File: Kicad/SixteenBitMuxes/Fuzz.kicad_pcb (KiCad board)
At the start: 2 copper layers, 100 x 82 mm, 109 parts, among them J1 Audio In/Out JST XH, J10 Key Pad JST XH, J11 LCD JST XH, J12 Bypass Switch JST XH, J2 POT B10K JST XH, J3 POT B5K JST XH, J4 VOL POT A100K JST XH, J5 PowerTest_PinHeader, J6 9V Power JST XH, J7 Boot Reset PinHeader, J9 SWD_PinHeader, Q1 PN2222A, Q10 2SC1815, Q11 PN2222A, Q12 S9013, Q13 MMBT3904, Q14 S9018, Q15 BC848B, Q16 2SC1623, Q17 MPSA18, Q18 MMBT5551L, Q19 2N5088, Q2 MMBT3904, Q20 MMBTA42, Q21 BC807, Q22 BC846, Q23 BC847B, Q24 BC847C, Q25 BC848B, Q26 S9013, Q27 S9018, Q28 C945, Q29 2SC1623, Q3 MMBT5551L, Q30 2SC1815, Q31 MPSA18, Q32 2N5088, Q4 MMBTA42, Q5 BC807, Q6 BC846, Q7 BC847B, Q8 BC847C, Q9 C945, U1 AMS1117-5.0, U2 AMS1117-3.3, U21 CD4051B, U22 4504, U23 4504, U24 4504, U25 CD4053B, U3 STM32F103C8Tx, U4 CD4051B, U6 CD4067BM, U7 CD4067BM, U8 CD4067BM, U9 CD4067BM, Y1 8MHz

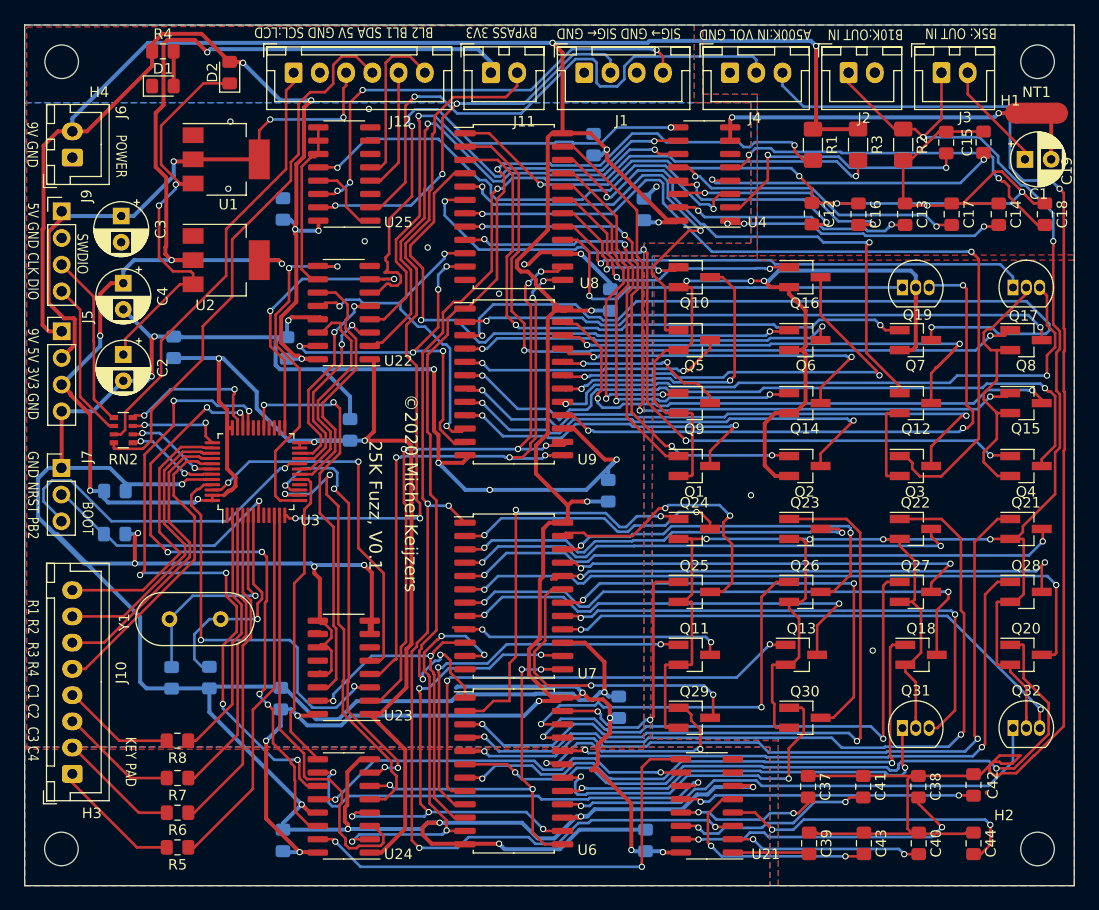
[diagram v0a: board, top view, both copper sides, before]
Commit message: LCD backlight and backlight removed from circuit/pcb.
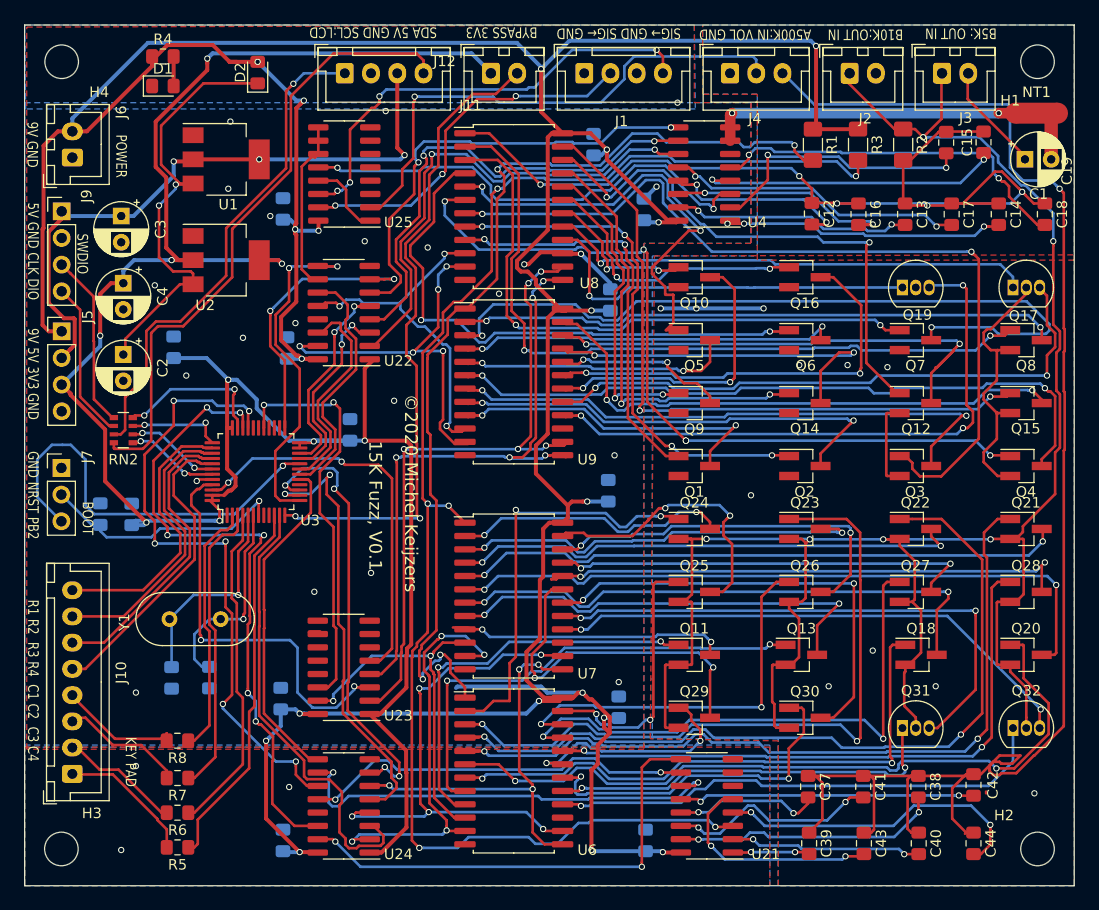
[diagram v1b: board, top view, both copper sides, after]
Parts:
- J11: footprint Connector_JST:JST_XH_B6B-XH-A_1x06_P2.50mm_Vertical -> Connector_JST:JST_XH_B4B-XH-A_1x04_P2.50mm_Vertical
- moved J11 4.87 mm to (60.5, 34.6)
- moved C7 2.74 mm to (40.2, 76.6), turned to 270 degrees
- moved D2 2.67 mm to (52.2, 34.5)
- moved C10 2.35 mm to (37.2, 76.6), turned to 90 degrees
- moved R4 0.49 mm to (43.2, 33.0)
- moved J2 0.11 mm to (108.6, 34.6)
- moved J3 0.08 mm to (117.4, 34.6)
- moved J1 0.06 mm to (83.3, 34.6)
- moved J12 0.06 mm to (74.4, 34.6)
- moved J4 0.06 mm to (97.2, 34.6)
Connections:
- U25 pad 4: /1602_BACK_LIGHT_PIN_1 -> Net-(U25-Pad4)
- U25 pad 5: /1602_BACK_LIGHT_PIN_2 -> Net-(U25-Pad5)
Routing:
- net GND: track 411.6 -> 43.4 mm, vias 30 -> 27
- net GNDA: track 124.8 -> 49.5 mm, vias 5 -> 11
- net /1602_BACK_LIGHT_PIN_2: track 15.8 -> 0.00 mm
- net /1602_BACK_LIGHT_PIN_1: track 12.0 -> 0.00 mm
- net /Mcu/PB2: track 32.4 -> 39.7 mm
- net /Mcu/I2C1_SDA: track 52.9 -> 60.0 mm
- net +5V: track 54.3 -> 60.7 mm
- net /CAPACITOR_A_SELECTION_2: track 49.6 -> 43.5 mm
- net /Mcu/I2C1_SCL: track 42.4 -> 47.6 mm, vias 0 -> 1
- net /CapacitorsD/CAPACITOR_AUDIO_OUTPUT: track 143.6 -> 148.6 mm
- net /CAPACITOR_A_SELECTION_0: track 52.1 -> 47.5 mm
- net /CAPACITOR_A_SELECTION_1: track 51.3 -> 46.7 mm
- net /JACK_OUT_SIGNAL_FROM_FUZZ: track 53.7 -> 49.5 mm
- net /TransistorsC/13_COLLECTOR: track 29.9 -> 33.9 mm
- net Net-(C38-Pad2): track 29.5 -> 25.5 mm
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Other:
- board text added: "15K Fuzz, V0.1"
- board text added: "SDA 5V GND SCL:LCD"
- board text removed: "25K Fuzz, V0.1"
- board text removed: "BL2 BL1 SDA 5V GND SCL:LCD"

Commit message: PCB Logo/texts
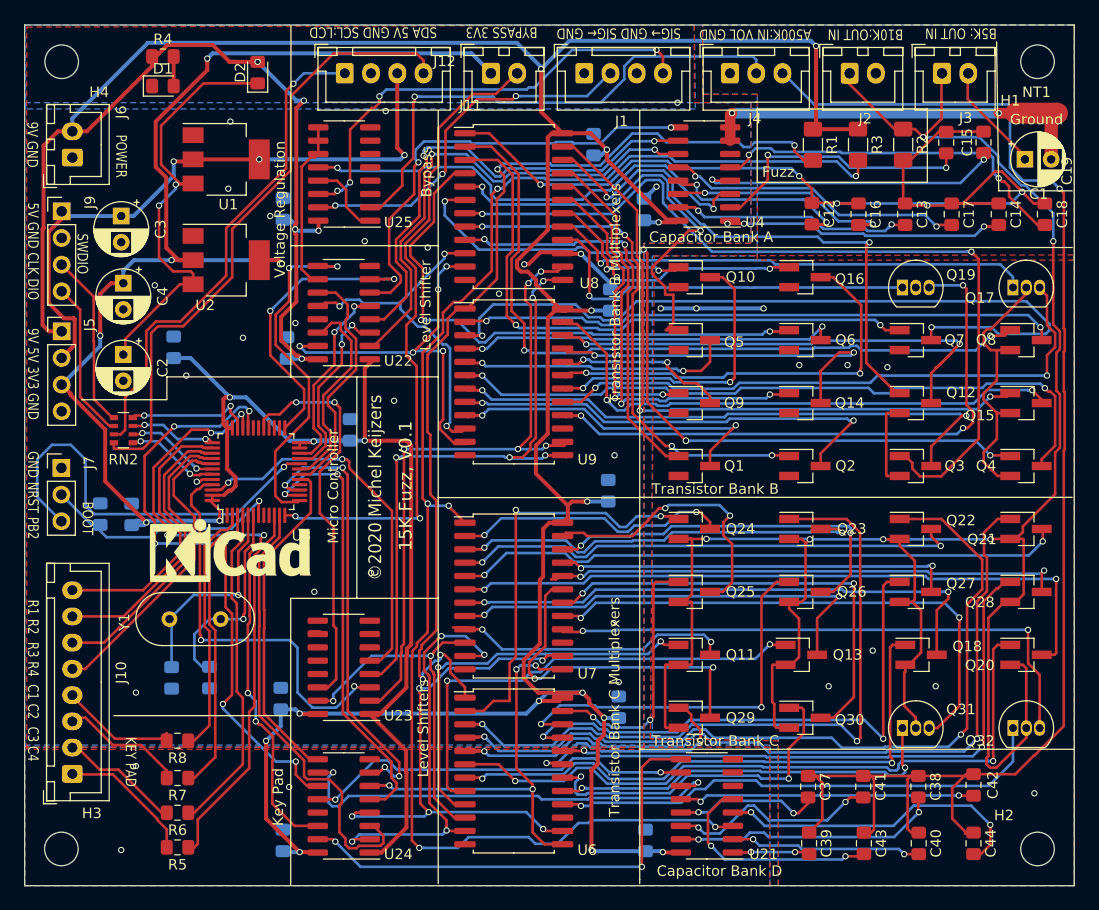
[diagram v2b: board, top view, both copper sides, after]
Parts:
- added REF**: KiCad-Logo_6mm_SilkScreen, Symbol:KiCad-Logo_6mm_SilkScreen, F.Cu at (49.6, 80.0)
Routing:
- net /TransistorsC/EMITTER: track 194.8 -> 210.0 mm
- net +9V: track 369.7 -> 359.4 mm
- net /CapacitorsD/CAPACITOR_AUDIO_OUTPUT: track 148.6 -> 140.8 mm
- net /TransistorsC/4_BASE: track 71.4 -> 66.0 mm
- net /TransistorsC/16_COLLECTOR: track 51.7 -> 54.6 mm
- net /TransistorsC/11_COLLECTOR: track 40.8 -> 38.1 mm
- net /Mcu/SYS_JTMS_SWDIO_MCU: track 14.7 -> 12.1 mm
- net /TransistorsC/15_COLLECTOR: track 53.2 -> 51.2 mm
- net /CAPACITOR_D_SELECTION_1_3V3: track 60.6 -> 58.7 mm
- net +3V3: track 213.4 -> 211.9 mm
- net /CAPACITOR_A_SELECTION_2_3V3: track 26.7 -> 28.2 mm
- net /TRANSISTOR_B_SELECTION_3_3V3: track 38.0 -> 36.5 mm
- net /TransistorsC/12_COLLECTOR: track 50.9 -> 49.9 mm
- net /TransistorsC/3_COLLECTOR: track 54.1 -> 53.1 mm
- net /TransistorsC/1_COLLECTOR: track 26.9 -> 27.8 mm
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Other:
- board text added: "Bypass"
- board text added: "Capacitor Bank A"
- board text added: "Capacitor Bank D"
- board text added: "Fuzz"
- board text added: "Ground"
- board text added: "Key Pad"
- board text added: "Level Shifter"
- board text added: "Level Shifters"
- board text added: "Micro Controller"
- board text added: "Transistor Bank B"
- board text added: "Transistor Bank B Multiplexers"
- board text added: "Transistor Bank C"
- board text added: "Transistor Bank C Multiplexers"
- board text added: "Voltage Regulation"

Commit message: EEprom + PCB changes
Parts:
- removed REF**: KiCad-Logo_6mm_SilkScreen, Symbol:KiCad-Logo_6mm_SilkScreen
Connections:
- U3 pad 30: Net-(U3-Pad30) -> /CAPACITOR_D_SELECTION_1_3V3
- U3 pad 31: Net-(U3-Pad31) -> /CAPACITOR_D_SELECTION_2_3V3
- U3 pad 32: /CAPACITOR_D_SELECTION_1_3V3 -> Net-(U3-Pad32)
- U3 pad 33: /CAPACITOR_D_SELECTION_2_3V3 -> Net-(U3-Pad33)
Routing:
- net /CAPACITOR_D_SELECTION_2_3V3: track 61.0 -> 62.3 mm
- net /CAPACITOR_D_SELECTION_1_3V3: track 58.7 -> 59.8 mm

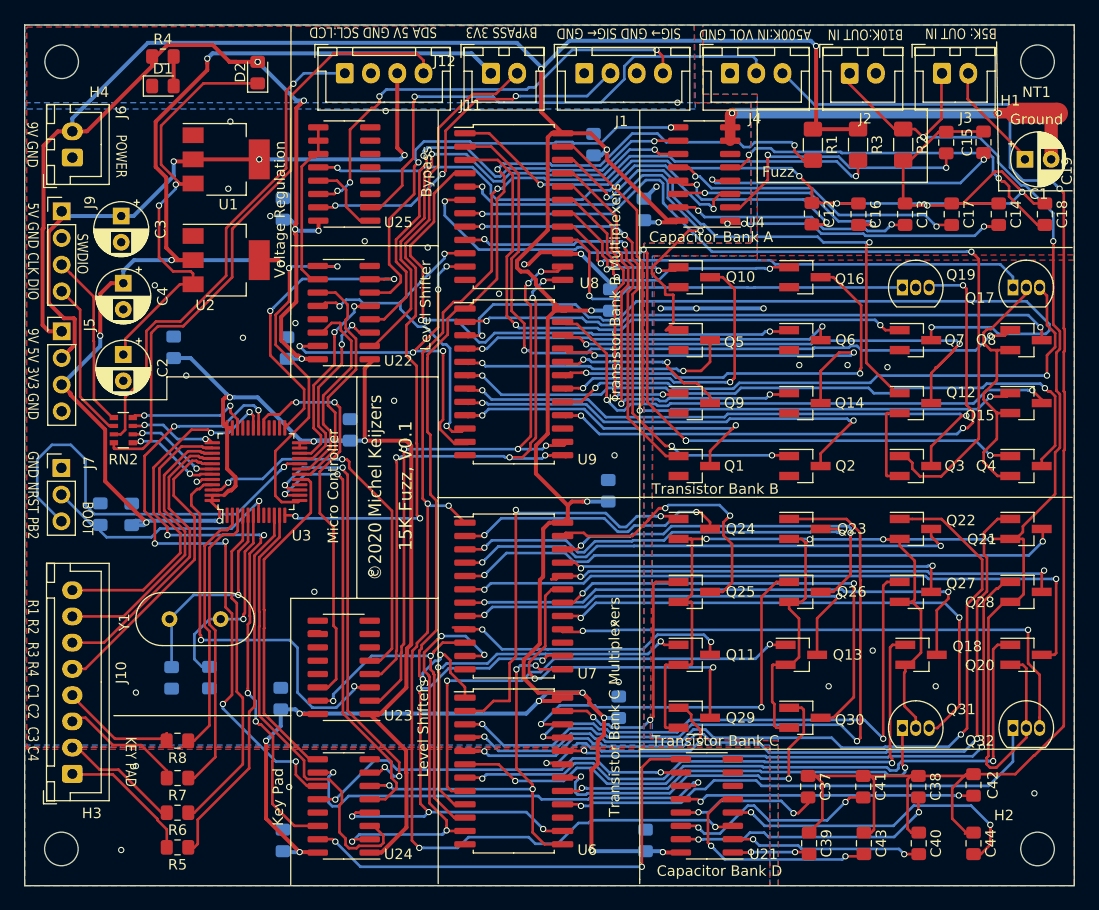
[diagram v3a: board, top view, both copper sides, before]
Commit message: logo, capacitors
Logo, removed capacitors location, added fuz capcitors to back. TODO: change capacitors bank A.
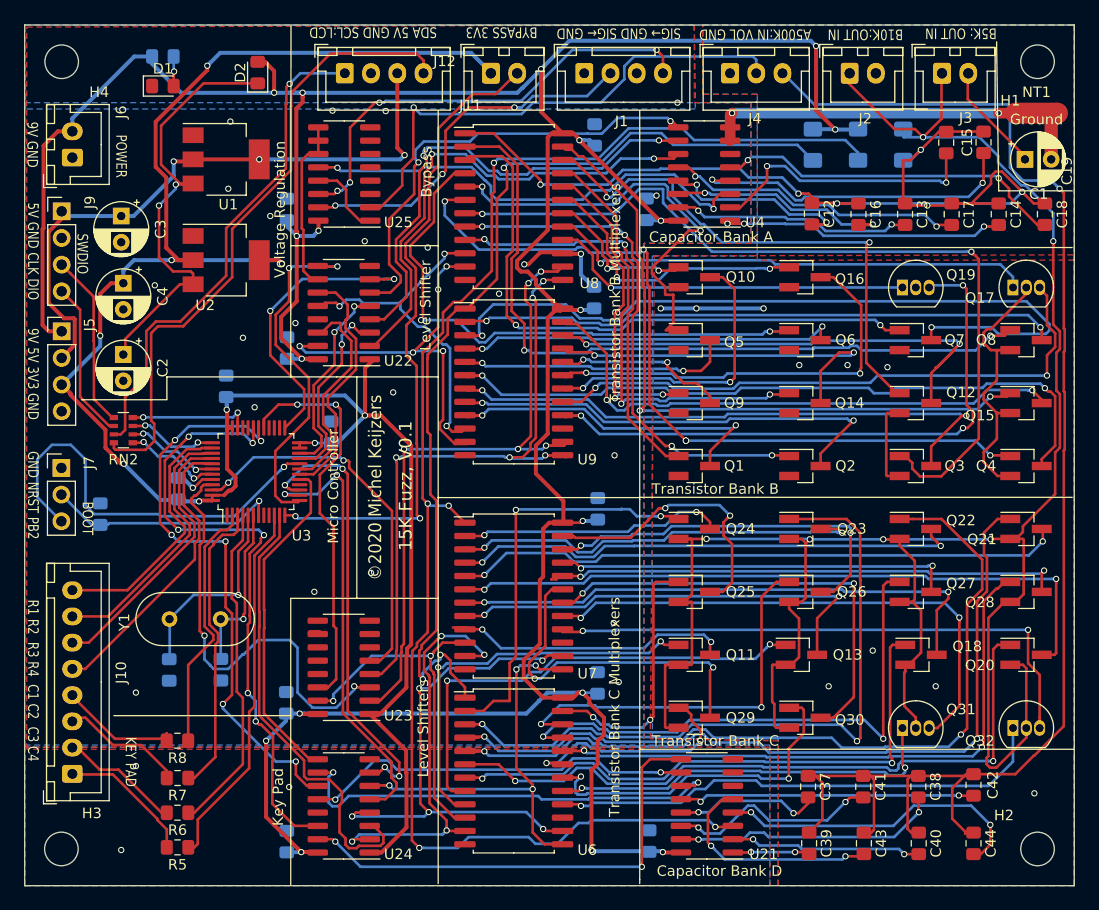
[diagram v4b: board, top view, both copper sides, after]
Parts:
- added REF**: KiCad-Logo2_30mm_SilkScreen, Symbol:KiCad-Logo2_30mm_SilkScreen, B.Cu at (89.4, 72.2)
- C19, C44: value C -> 42uF
- R1, R2, R3, R4: moved to B.Cu
- moved C8 6.23 mm to (49.2, 64.4)
- moved C7 5.06 mm to (44.6, 74.2)
- moved C21 3.07 mm to (84.6, 92.7)
- moved C22 1.99 mm to (84.6, 76.1)
- moved C9 1.81 mm to (59.2, 68.8)
- moved C23 1.57 mm to (84.2, 56.0)
- moved C6 1.33 mm to (48.7, 91.4)
- moved C24 0.93 mm to (84.3, 40.5)
- moved C5 0.79 mm to (43.8, 91.4)
- moved C48 0.66 mm to (54.9, 94.6)
- moved C45 0.39 mm to (55.0, 47.6)
- moved C46 0.38 mm to (55.0, 107.8)
- moved C36 0.35 mm to (89.5, 107.8)
- moved C11 0.24 mm to (89.2, 47.6)
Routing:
- net +9V: track 359.4 -> 331.8 mm, vias 19 -> 18
- net +3V3: track 211.9 -> 196.0 mm
- net /CAPACITOR_D_SELECTION_1_3V3: track 59.8 -> 55.6 mm
- net /TRANSISTOR_B_SELECTION_2_3V3: track 39.0 -> 42.4 mm
- net Net-(C6-Pad1): track 19.6 -> 16.8 mm
- net /CAPACITOR_D_SELECTION_2_3V3: track 62.3 -> 59.6 mm
- net /TransistorsC/EMITTER: track 210.0 -> 212.6 mm
- net Net-(C19-Pad2): track 29.3 -> 31.9 mm
- net /TransistorsB/16_BASE: track 37.6 -> 35.1 mm
- net /CapacitorsD/CAPACITOR_AUDIO_INPUT: track 141.4 -> 143.5 mm, vias 6 -> 5
- net Net-(C18-Pad2): track 35.4 -> 33.5 mm
- net /Mcu/GPIO_KEYPAD_ROW_1: track 26.6 -> 24.7 mm
- net /TransistorsB/BASE: track 93.4 -> 95.1 mm, vias 5 -> 6
- net /Mcu/GPIO_KEYPAD_ROW_3: track 28.1 -> 26.4 mm
- net /Mcu/GPIO_KEYPAD_ROW_2: track 27.2 -> 25.6 mm
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
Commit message: PCB and code
Some PCB changes.
HalUtils, multiplexer code, component code.
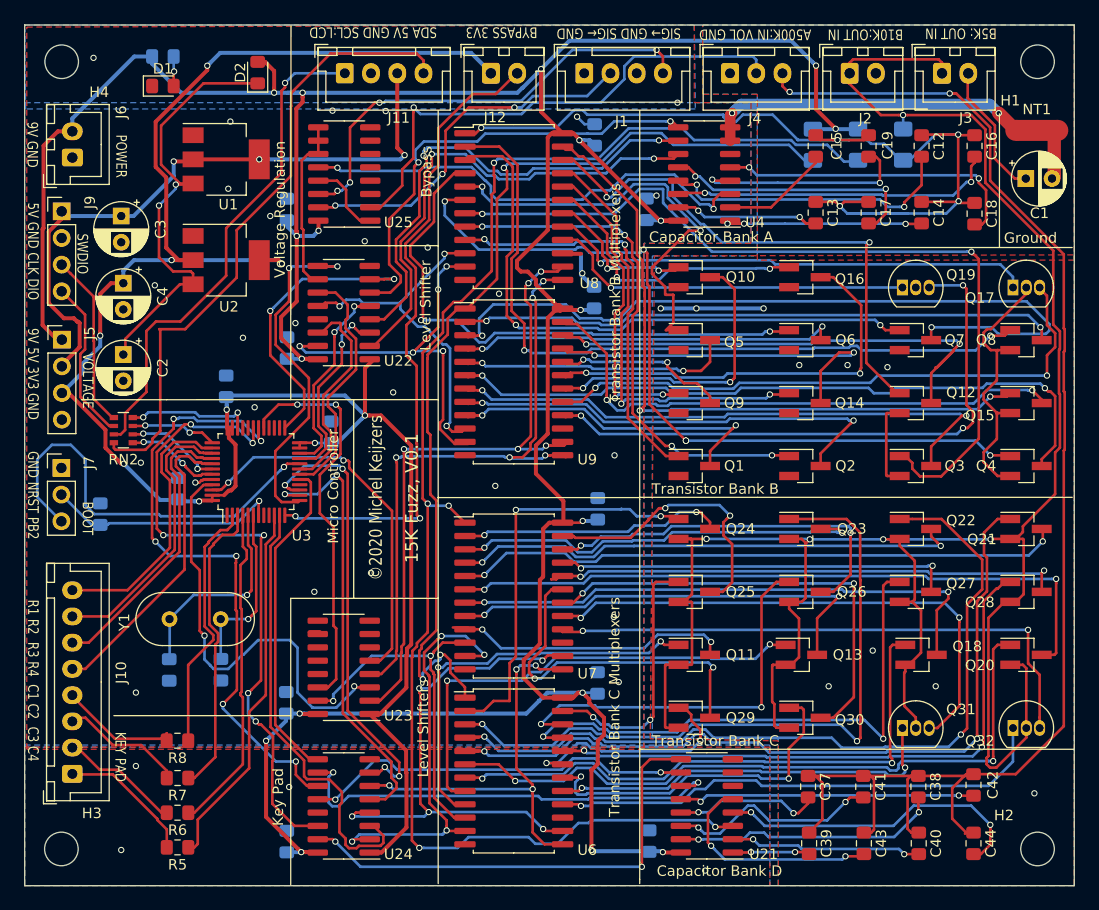
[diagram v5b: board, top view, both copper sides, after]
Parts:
- moved C16 12.8 mm to (120.5, 41.5)
- moved C15 12.4 mm to (105.4, 41.5)
- moved C12 12.3 mm to (115.5, 41.5)
- moved C19 11.0 mm to (110.4, 41.5)
- moved C13 8.52 mm to (105.4, 47.9)
- moved C17 7.91 mm to (110.4, 47.9)
- moved C14 7.35 mm to (115.5, 47.9)
- moved C18 6.70 mm to (120.5, 48.0)
- moved REF** 5.60 mm to (89.5, 77.8)
- moved C1 1.83 mm to (125.4, 44.6)
- moved NT1 1.64 mm to (126.4, 40.0)
- moved J5 0.80 mm to (33.5, 60.0)
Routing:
- net Net-(C15-Pad2): track 26.5 -> 10.5 mm, vias 2 -> 0
- net Net-(C12-Pad2): track 17.8 -> 28.6 mm
- net Net-(C19-Pad2): track 31.9 -> 21.2 mm
- net Net-(C13-Pad2): track 22.8 -> 13.7 mm
- net Net-(C16-Pad2): track 22.6 -> 31.1 mm
- net Net-(C14-Pad2): track 26.7 -> 18.5 mm
- net /TransistorsC/EMITTER: track 212.6 -> 216.9 mm, vias 6 -> 5
- net /CAPACITOR_D_SELECTION_1_3V3: track 55.6 -> 59.6 mm
- net Net-(C18-Pad2): track 33.5 -> 29.7 mm
- net Net-(C17-Pad2): track 28.6 -> 25.2 mm
- net /CAPACITOR_D_SELECTION_2_3V3: track 59.6 -> 63.0 mm
- net /CapacitorsD/CAPACITOR_AUDIO_OUTPUT: track 140.8 -> 137.6 mm, vias 1 -> 2
- net GND: track 44.7 -> 41.9 mm, vias 29 -> 33
- net Net-(C1-Pad1): track 10.5 -> 13.0 mm
- net /TransistorsB/BASE: track 95.1 -> 96.8 mm, vias 6 -> 5
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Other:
- net class I2C added: clearance 0.2, trace_width 0.254, via_dia 0.6, via_drill 0.4
- board text added: "VOLTAGE"
